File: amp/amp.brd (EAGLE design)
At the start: 99.1 x 80 mm, 69 parts, among them IC1 OPA2134PA, Q1 BC547, Q10 IRF510, Q11 BC556, Q12 BC556, Q13 BC547, Q14 BC547, Q15 2N7000, Q16 BC547, Q17 BC547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

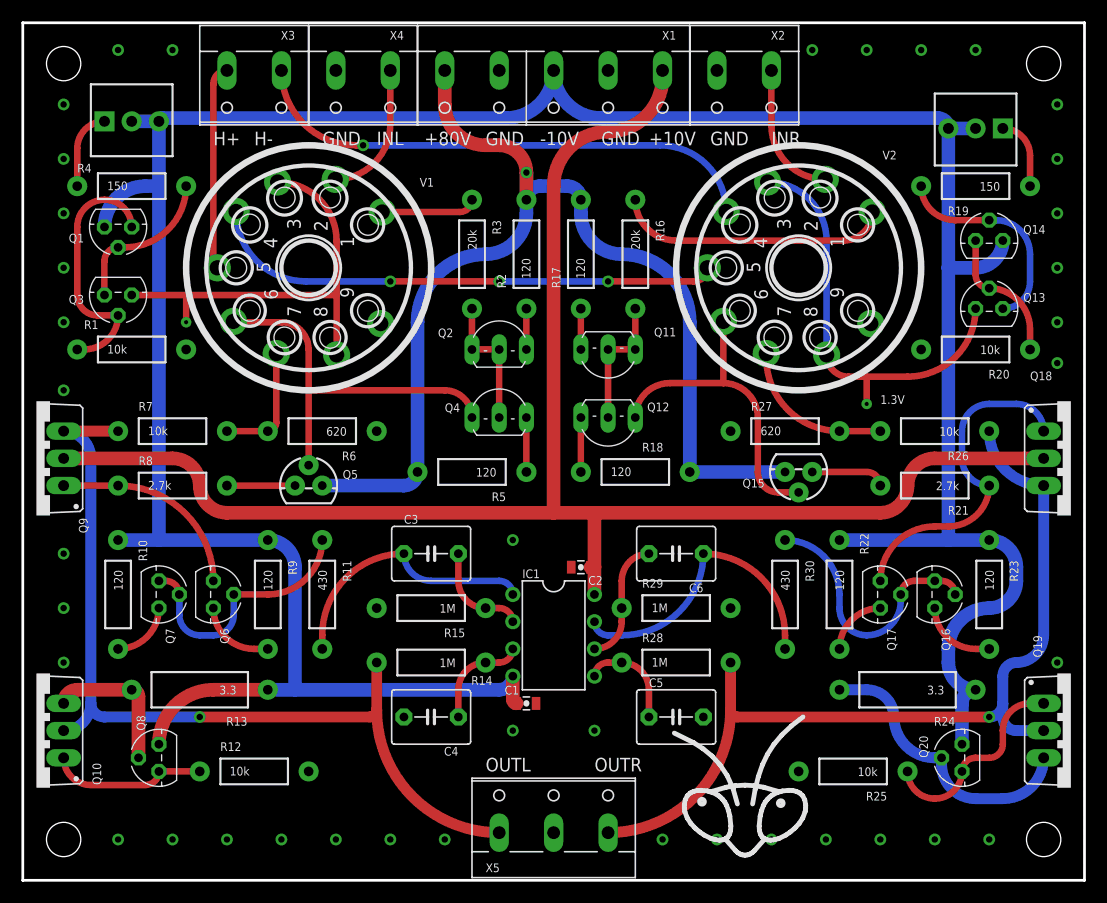
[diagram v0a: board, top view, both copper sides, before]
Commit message: Back to 60V supply
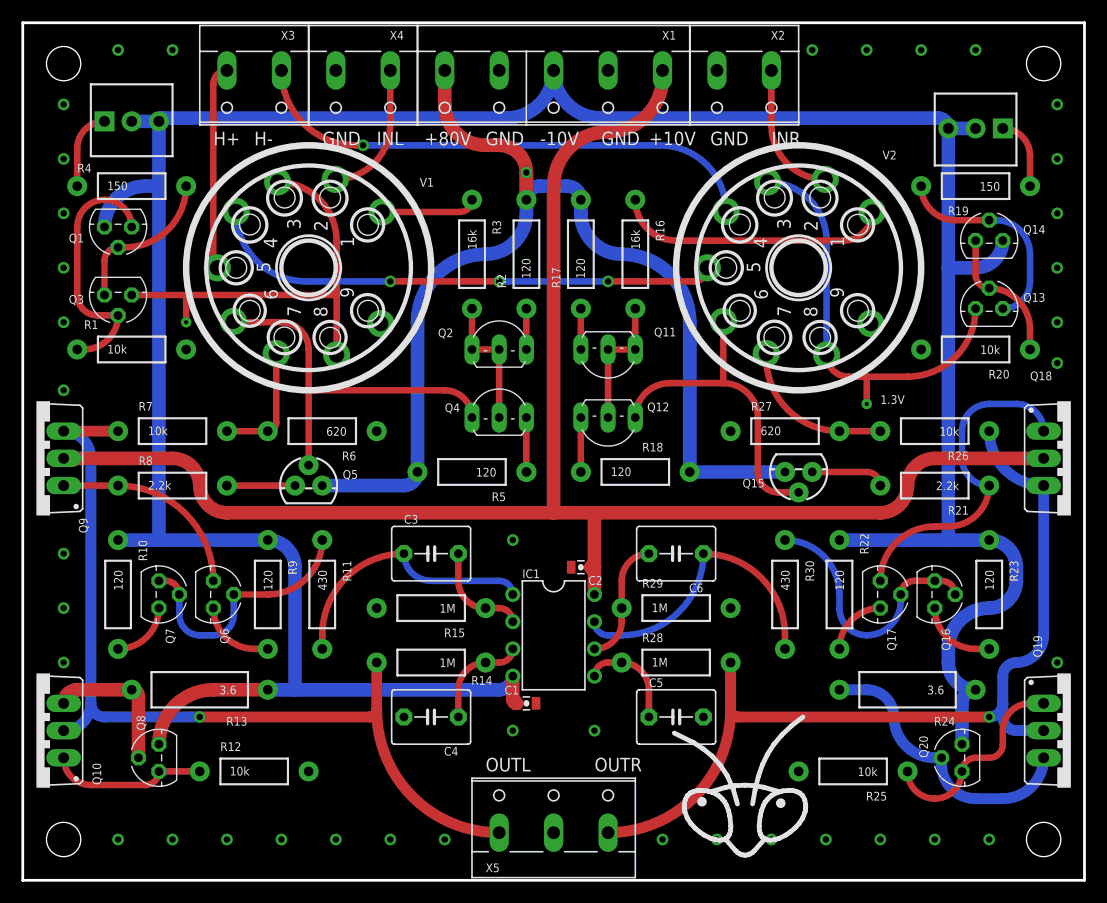
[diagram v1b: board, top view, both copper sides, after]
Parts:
- R13, R24: value 3.3 -> 3.6
- R16, R3: value 20k -> 16k
- R21, R8: value 2.7k -> 2.2k
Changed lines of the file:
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@@
 <attribute name="VALUE" x="5.715" y="61.595" size="0.8128" layer="27" ratio="15" rot="R180"/>
 </element>
-<element name="R3" library="SparkFun-Resistors" package="AXIAL-0.4" value="20k" x="41.91" y="58.42" rot="R270"/>
+<element name="R3" library="SparkFun-Resistors" package="AXIAL-0.4" value="16k" x="41.91" y="58.42" rot="R270"/>
 <element name="R2" library="SparkFun-Resistors" package="AXIAL-0.4" value="120" x="46.99" y="58.42" smashed="yes" rot="R90">
 <attribute name="NAME" x="45.085" y="55.245" size="0.8128" layer="25" font="vector" ratio="15" rot="R90"/>
@@
 <attribute name="VALUE" x="29.845" y="35.56" size="0.8128" layer="27" ratio="15"/>
 </element>
-<element name="R8" library="SparkFun-Resistors" package="AXIAL-0.4" value="2.7k" x="13.97" y="36.83"/>
+<element name="R8" library="SparkFun-Resistors" package="AXIAL-0.4" value="2.2k" x="13.97" y="36.83"/>
 <element name="Q7" library="transistor-npn" package="TO92" value="BC547" x="12.7" y="26.67" smashed="yes" rot="R270">
 <attribute name="NAME" x="13.335" y="23.495" size="0.8128" layer="25" ratio="15" rot="R270"/>
@@
 <attribute name="VALUE" x="15.875" y="11.43" size="0.8128" layer="27" ratio="15" rot="R90"/>
 </element>
-<element name="R13" library="SparkFun-Resistors" package="AXIAL-0.5" value="3.3" x="16.51" y="17.78" smashed="yes" rot="R180">
+<element name="R13" library="SparkFun-Resistors" package="AXIAL-0.5" value="3.6" x="16.51" y="17.78" smashed="yes" rot="R180">
 <attribute name="NAME" x="20.955" y="15.24" size="0.8128" layer="25" font="vector" ratio="15" rot="R180"/>
 <attribute name="VALUE" x="19.939" y="18.161" size="0.8128" layer="21" font="vector" ratio="15" rot="R180"/>
@@
 <attribute name="VALUE" x="62.23" y="43.307" size="0.8128" layer="27" ratio="15" rot="R180"/>
 </element>
-<element name="R16" library="SparkFun-Resistors" package="AXIAL-0.4" value="20k" x="57.15" y="58.42" rot="R270"/>
+<element name="R16" library="SparkFun-Resistors" package="AXIAL-0.4" value="16k" x="57.15" y="58.42" rot="R270"/>
 <element name="R17" library="SparkFun-Resistors" package="AXIAL-0.4" value="120" x="52.07" y="58.42" rot="R90"/>
 <element name="R18" library="SparkFun-Resistors" package="AXIAL-0.4" value="120" x="57.15" y="38.1" smashed="yes">
@@
 <attribute name="VALUE" x="69.215" y="39.37" size="0.8128" layer="27" ratio="15" rot="R180"/>
 </element>
-<element name="R21" library="SparkFun-Resistors" package="AXIAL-0.4" value="2.7k" x="85.09" y="36.83" rot="R180"/>
+<element name="R21" library="SparkFun-Resistors" package="AXIAL-0.4" value="2.2k" x="85.09" y="36.83" rot="R180"/>
 <element name="Q16" library="transistor-npn" package="TO92" value="BC547" x="85.09" y="26.67" smashed="yes" rot="R270">
 <attribute name="NAME" x="85.725" y="23.495" size="0.8128" layer="25" ratio="15" rot="R270"/>
@@
 <attribute name="VALUE" x="90.805" y="10.16" size="0.8128" layer="27" ratio="15" rot="R90"/>
 </element>
-<element name="R24" library="SparkFun-Resistors" package="AXIAL-0.5" value="3.3" x="82.55" y="17.78" smashed="yes" rot="R180">
+<element name="R24" library="SparkFun-Resistors" package="AXIAL-0.5" value="3.6" x="82.55" y="17.78" smashed="yes" rot="R180">
 <attribute name="NAME" x="86.995" y="15.24" size="0.8128" layer="25" font="vector" ratio="15" rot="R180"/>
 <attribute name="VALUE" x="85.979" y="18.161" size="0.8128" layer="21" font="vector" ratio="15" rot="R180"/>

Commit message: HV for neon bulb
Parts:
- V1, V2: value (none) -> 6922
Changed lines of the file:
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@@
 <wire x1="99.06" y1="0" x2="0" y2="0" width="0.254" layer="20"/>
 <wire x1="0" y1="0" x2="0" y2="80.01" width="0.254" layer="20"/>
-<dimension x1="0" y1="80.01" x2="0" y2="0" x3="-5.08" y3="40.005" textsize="1.778" layer="47"/>
+<dimension x1="0" y1="80.01" x2="0" y2="0" x3="-5.08" y3="40.005" textsize="1.27" layer="47"/>
 <text x="33.02" y="68.58" size="1.27" layer="21" font="vector" ratio="15">INL</text>
 <text x="17.78" y="68.58" size="1.27" layer="21" font="vector" ratio="15">H+</text>
@@
 <text x="53.34" y="10.16" size="1.27" layer="21" font="vector" ratio="15">OUTR</text>
 <text x="80.01" y="44.45" size="0.8128" layer="21" font="vector" ratio="15">1.3V</text>
-<dimension x1="0" y1="80.01" x2="99.06" y2="80.01" x3="49.53" y3="85.09" textsize="1.27" layer="47"/>
+<dimension x1="0" y1="80.01" x2="99.06" y2="80.01" x3="49.53" y3="87.63" textsize="1.27" layer="47"/>
 <text x="27.94" y="68.58" size="1.27" layer="21" font="vector" ratio="15">GND</text>
 <text x="43.18" y="68.58" size="1.27" layer="21" font="vector" ratio="15">GND</text>
 <text x="53.975" y="68.58" size="1.27" layer="21" font="vector" ratio="15">GND</text>
 <text x="64.135" y="68.58" size="1.27" layer="21" font="vector" ratio="15">GND</text>
+<dimension x1="0" y1="80.01" x2="49.53" y2="80.01" x3="24.765" y3="85.09" textsize="1.27" layer="47"/>
+<dimension x1="0" y1="80.01" x2="21.59" y2="80.01" x3="10.795" y3="82.55" textsize="1.27" layer="47"/>
 </plain>
 <attributes>
@@
 <attribute name="VALUE" x="7.874" y="49.149" size="0.8128" layer="21" font="vector" ratio="15"/>
 </element>
-<element name="V1" library="tubes" package="NOVAL" value="" x="26.67" y="57.15" smashed="yes" rot="R90">
+<element name="V1" library="tubes" package="NOVAL" value="6922" x="26.67" y="57.15" smashed="yes" rot="R90">
 <attribute name="NAME" x="38.354" y="65.532" size="0.8128" layer="25" ratio="15" rot="R180"/>
 <attribute name="VALUE" x="43.688" y="53.086" size="1.778" layer="27" ratio="10" rot="R90"/>
@@
 <attribute name="NAME" x="43.18" y="0.762" size="0.8128" layer="25" ratio="15"/>
 </element>
-<element name="V2" library="tubes" package="NOVAL" value="" x="72.39" y="57.15" smashed="yes" rot="R90">
+<element name="V2" library="tubes" package="NOVAL" value="6922" x="72.39" y="57.15" smashed="yes" rot="R90">
 <attribute name="NAME" x="81.534" y="68.072" size="0.8128" layer="25" ratio="15" rot="R180"/>
 <attribute name="VALUE" x="89.408" y="53.086" size="1.778" layer="27" ratio="10" rot="R90"/>

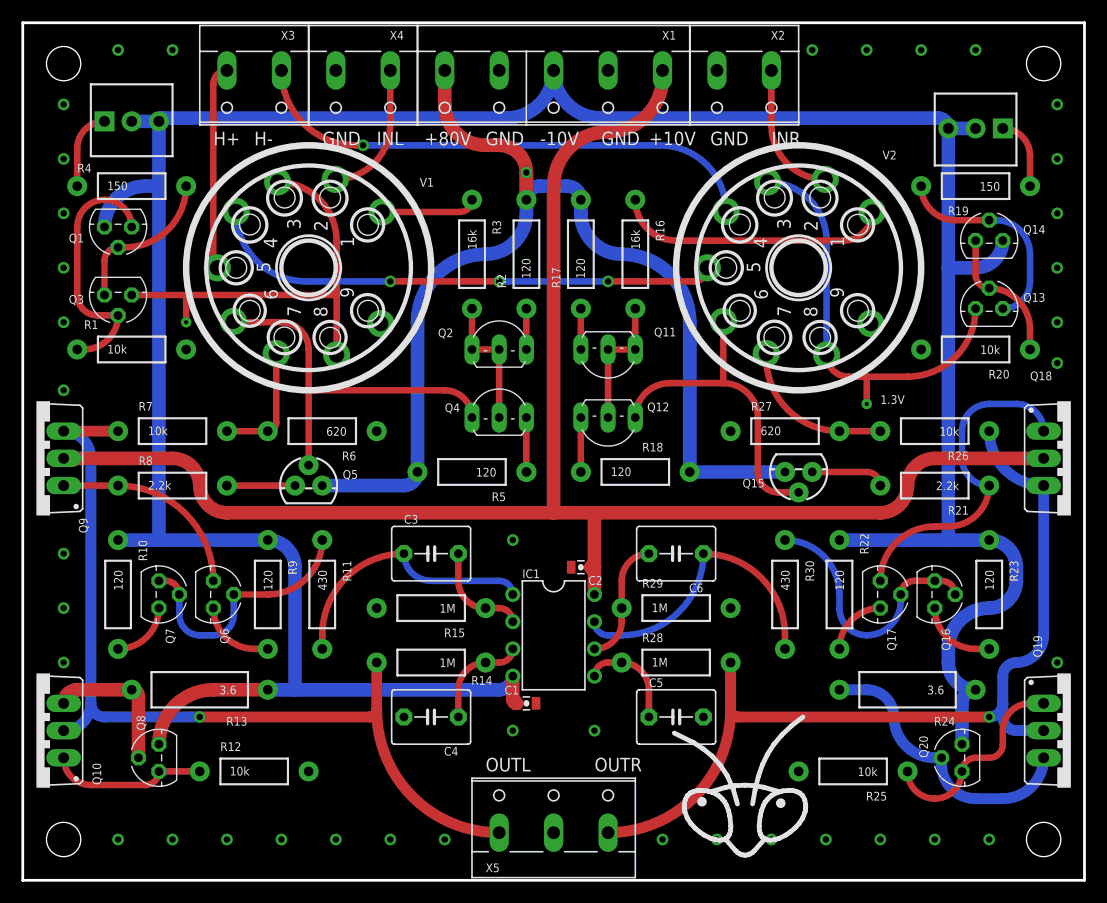
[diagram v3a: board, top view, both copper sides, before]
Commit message: Gate resistors added
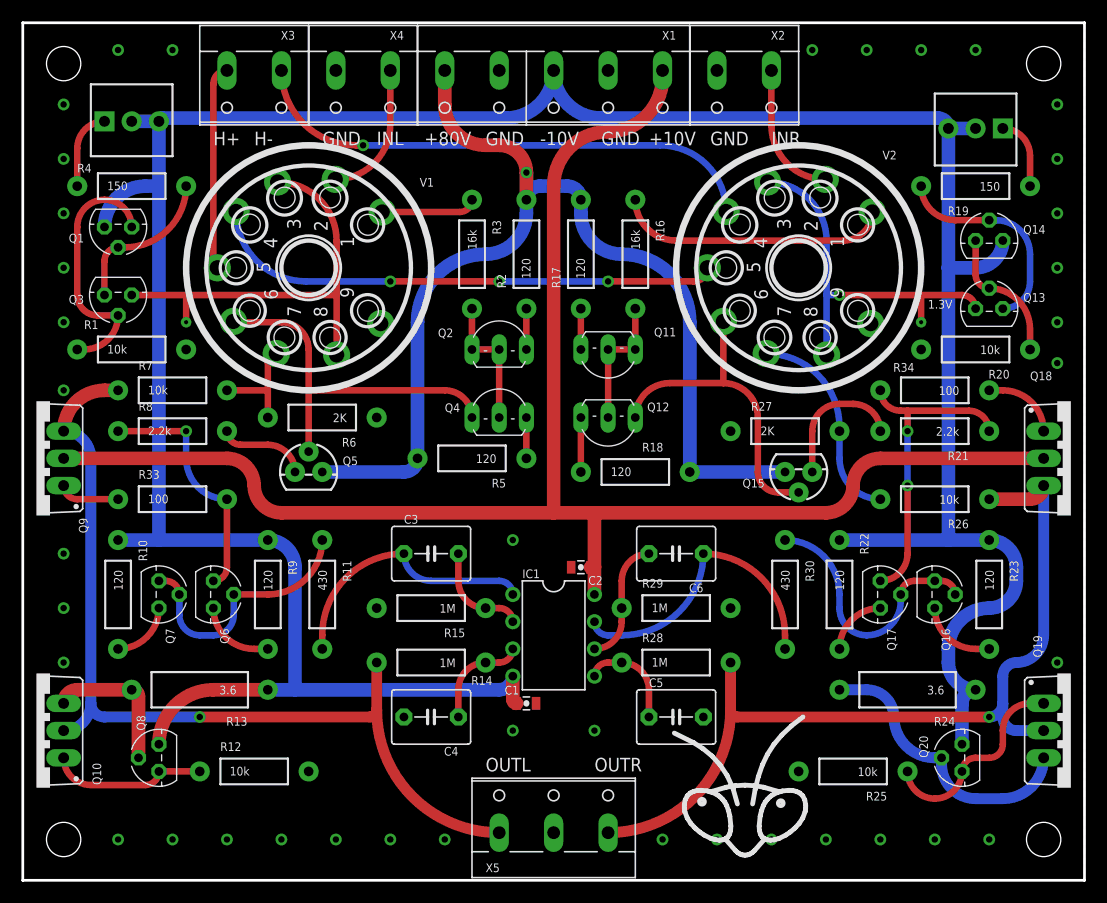
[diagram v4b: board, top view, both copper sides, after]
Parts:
- added R33, R34: 100, SparkFun-Resistors:AXIAL-0.4
- Q10, Q18, Q19, Q9: value IRF510 -> IRF610
- R27, R6: value 620 -> 2K
- moved TP1 9.16 mm to (83.8, 52.1)
- moved R26 6.35 mm to (85.1, 35.6)
- moved R21 5.08 mm to (85.1, 41.9)
- moved R8 5.08 mm to (14.0, 41.9)
- moved R7 3.81 mm to (14.0, 45.7)
- moved Q5 1.27 mm to (26.7, 38.1)
- moved R6 1.27 mm to (27.9, 43.2)
- moved R5 1.27 mm to (41.9, 39.4)
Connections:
- new net N$41: Q9.1, R33.P$1
- new net N$42: Q18.1, R34.P$1
- net N$13: now also R33.P$2; no longer Q9.G
- net N$15: now also Q10.1; no longer Q10.G
- net N$16: now also Q10.3; no longer Q10.S
- net N$31: now also R34.P$2; no longer Q18.G
- net N$33: now also Q19.1; no longer Q19.G
- net N$34: now also Q19.3; no longer Q19.S
- net OUTL: now also Q10.2, Q9.3; no longer Q10.D, Q9.S
- net OUTR: now also Q18.3, Q19.2; no longer Q18.S, Q19.D
- net VCC: now also Q18.2, Q9.2; no longer Q18.D, Q9.D
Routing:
- net N$42: track 0.00 -> 6.66 mm
- net N$41: track 0.00 -> 5.61 mm
- net N$32: track 6.88 -> 12.3 mm
- net N$13: track 17.7 -> 22.4 mm, vias 0 -> 1
- net N$35: track 13.9 -> 18.0 mm
- net N$18: track 38.3 -> 35.4 mm, vias 0 -> 1
- net OUTR: track 81.5 -> 79.9 mm
- net OUTL: track 83.2 -> 84.8 mm
- net N$14: track 6.35 -> 7.93 mm
- net N$4: track 35.2 -> 33.9 mm
- net HT: track 102.2 -> 100.9 mm
- net N$9: track 11.4 -> 10.1 mm
- net N$6: track 5.08 -> 3.81 mm
- net N$31: track 29.7 -> 28.7 mm, vias 0 -> 2

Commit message: Back to IRF5xx
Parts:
- Q10, Q18, Q19, Q9: value IRF610 -> IRF540; device my:TO220BV -> transistor-power:TO220BV
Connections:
- net N$15: now also Q10.G; no longer Q10.1
- net N$16: now also Q10.S; no longer Q10.3
- net N$33: now also Q19.G; no longer Q19.1
- net N$34: now also Q19.S; no longer Q19.3
- net N$41: now also Q9.G; no longer Q9.1
- net N$42: now also Q18.G; no longer Q18.1
- net OUTL: now also Q10.D, Q9.S; no longer Q10.2, Q9.3
- net OUTR: now also Q18.S, Q19.D; no longer Q18.3, Q19.2
- net VCC: now also Q18.D, Q9.D; no longer Q18.2, Q9.2
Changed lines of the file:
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@@
 <attribute name="VALUE" x="8.509" y="28.956" size="0.8128" layer="21" font="vector" ratio="15" rot="R270"/>
 </element>
-<element name="Q9" library="my" package="TO220BV" value="IRF610" x="1.27" y="39.37" smashed="yes" rot="R90">
+<element name="Q9" library="transistor-power" package="TO220BV" value="IRF540" x="1.27" y="39.37" smashed="yes" rot="R90">
 <attribute name="NAME" x="6.0452" y="32.385" size="0.8128" layer="25" ratio="15" rot="R90"/>
 <attribute name="VALUE" x="7.62" y="32.385" size="0.8128" layer="27" ratio="15" rot="R90"/>
 </element>
-<element name="Q10" library="my" package="TO220BV" value="IRF610" x="1.27" y="13.97" smashed="yes" rot="R90">
+<element name="Q10" library="transistor-power" package="TO220BV" value="IRF540" x="1.27" y="13.97" smashed="yes" rot="R90">
 <attribute name="NAME" x="7.3152" y="8.89" size="0.8128" layer="25" ratio="15" rot="R90"/>
 <attribute name="VALUE" x="8.89" y="8.89" size="0.8128" layer="27" ratio="15" rot="R90"/>
@@
 </element>
 <element name="R23" library="SparkFun-Resistors" package="AXIAL-0.4" value="120" x="90.17" y="26.67" rot="R270"/>
-<element name="Q18" library="my" package="TO220BV" value="IRF610" x="97.79" y="39.37" smashed="yes" rot="R270">
+<element name="Q18" library="transistor-power" package="TO220BV" value="IRF540" x="97.79" y="39.37" smashed="yes" rot="R270">
 <attribute name="NAME" x="93.98" y="46.6598" size="0.8128" layer="25" ratio="15"/>
 <attribute name="VALUE" x="93.98" y="45.085" size="0.8128" layer="27" ratio="15"/>
 </element>
-<element name="Q19" library="my" package="TO220BV" value="IRF610" x="97.79" y="13.97" smashed="yes" rot="R270">
+<element name="Q19" library="transistor-power" package="TO220BV" value="IRF540" x="97.79" y="13.97" smashed="yes" rot="R270">
 <attribute name="NAME" x="94.2848" y="22.86" size="0.8128" layer="25" ratio="15" rot="R270"/>
 <attribute name="VALUE" x="92.71" y="24.13" size="0.8128" layer="27" ratio="15" rot="R270"/>
@@
 <contactref element="R12" pad="P$1"/>
 <contactref element="Q8" pad="3"/>
-<contactref element="Q10" pad="1"/>
+<contactref element="Q10" pad="G"/>
 <wire x1="12.7" y1="10.16" x2="16.51" y2="10.16" width="0.6096" layer="1"/>
 <wire x1="3.81" y1="11.43" x2="6.35" y2="8.89" width="0.6096" layer="1" curve="90"/>
@@
 </signal>
 <signal name="N$16" class="2">
-<contactref element="Q10" pad="3"/>
+<contactref element="Q10" pad="S"/>
 <contactref element="R13" pad="P$2"/>
 <contactref element="Q8" pad="2"/>
@@
 </signal>
 <signal name="OUTL" class="2">
-<contactref element="Q9" pad="3"/>
-<contactref element="Q10" pad="2"/>
+<contactref element="Q9" pad="S"/>
+<contactref element="Q10" pad="D"/>
 <contactref element="R7" pad="P$1"/>
 <contactref element="R14" pad="P$2"/>
@@
 </signal>
 <signal name="VCC" class="1">
-<contactref element="Q9" pad="2"/>
+<contactref element="Q9" pad="D"/>
 <contactref element="IC1" pad="8"/>
 <contactref element="C2" pad="1"/>
@@
 <wire x1="52.97" y1="29.21" x2="53.34" y2="29.21" width="1.27" layer="1"/>
 <wire x1="49.53" y1="64.77" x2="49.53" y2="34.29" width="1.27" layer="1"/>
-<contactref element="Q18" pad="2"/>
+<contactref element="Q18" pad="D"/>
 <wire x1="95.25" y1="39.37" x2="80.01" y2="39.37" width="1.27" layer="1"/>
 <wire x1="74.93" y1="34.29" x2="53.34" y2="34.29" width="1.27" layer="1"/>
@@
 <signal name="OUTR" class="2">
 <contactref element="X5" pad="3"/>
-<contactref element="Q18" pad="3"/>
-<contactref element="Q19" pad="2"/>
+<contactref element="Q18" pad="S"/>
+<contactref element="Q19" pad="D"/>
 <contactref element="R26" pad="P$1"/>
 <contactref element="R28" pad="P$2"/>
@@
 <contactref element="R25" pad="P$1"/>
 <contactref element="Q20" pad="3"/>
-<contactref element="Q19" pad="1"/>
+<contactref element="Q19" pad="G"/>
 <wire x1="82.55" y1="10.16" x2="85.09" y2="7.62" width="0.6096" layer="1" curve="90"/>
 <wire x1="85.09" y1="7.62" x2="87.63" y2="10.16" width="0.6096" layer="1" curve="90"/>
@@
 </signal>
 <signal name="N$34" class="2">
-<contactref element="Q19" pad="3"/>
+<contactref element="Q19" pad="S"/>
 <contactref element="R24" pad="P$2"/>
 <contactref element="Q20" pad="2"/>
@@
 </signal>
 <signal name="N$41">
-<contactref element="Q9" pad="1"/>
+<contactref element="Q9" pad="G"/>
 <contactref element="R33" pad="P$1"/>
 <wire x1="8.89" y1="35.56" x2="5.08" y2="35.56" width="0.6096" layer="1"/>
@@
 </signal>
 <signal name="N$42">
-<contactref element="Q18" pad="1"/>
+<contactref element="Q18" pad="G"/>
 <contactref element="R34" pad="P$1"/>
 <wire x1="90.17" y1="45.72" x2="91.44" y2="45.72" width="0.6096" layer="1"/>
